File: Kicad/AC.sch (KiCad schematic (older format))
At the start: 12 parts, among them U5 MCP6244

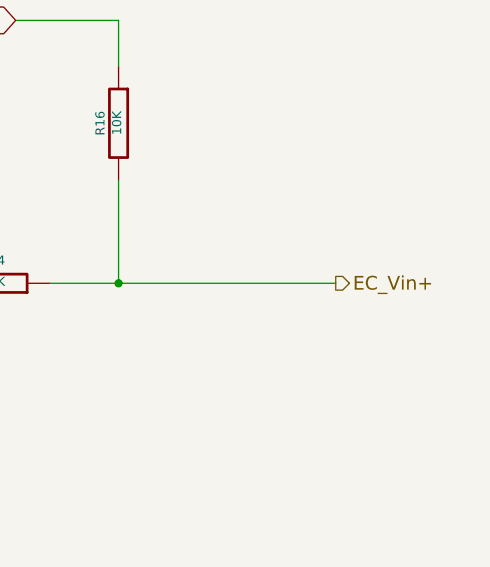
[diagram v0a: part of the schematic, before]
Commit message: iPhone app and changes to hw design (not sure I like)
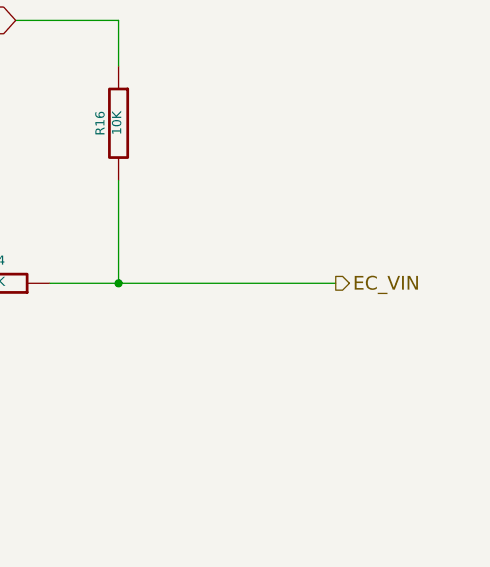
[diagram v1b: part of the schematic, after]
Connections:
- net EC_Vin+ renamed EC_VIN
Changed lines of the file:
@@
 $Descr A4 11693 8268
 encoding utf-8
-Sheet 6 11
+Sheet 6 9
 Title ""
-Date "9 feb 2015"
+Date "17 mar 2015"
 Rev ""
 Comp ""
@@
 VGND
 Text HLabel 8400 3850 2    60   Output ~ 0
-EC_Vin+
+EC_VIN
 $EndSCHEMATC
